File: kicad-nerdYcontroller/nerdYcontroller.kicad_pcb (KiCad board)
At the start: 4 copper layers, 69.8 x 35.2 mm, 124 parts, among them J201 S2B-PH-SM4-TB, J301 Conn_02x03_Odd_Even, J302 Conn_02x03_Odd_Even, J303 ZX-HY2.0-4PLT, J304 HLE-115-02-F-DV, P201 USB_C_Plug_USB2.0, Q301 DDTC113ZCA, U101 RP2040, U102 W25Q128JVS, U201 AMS1117-3.3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

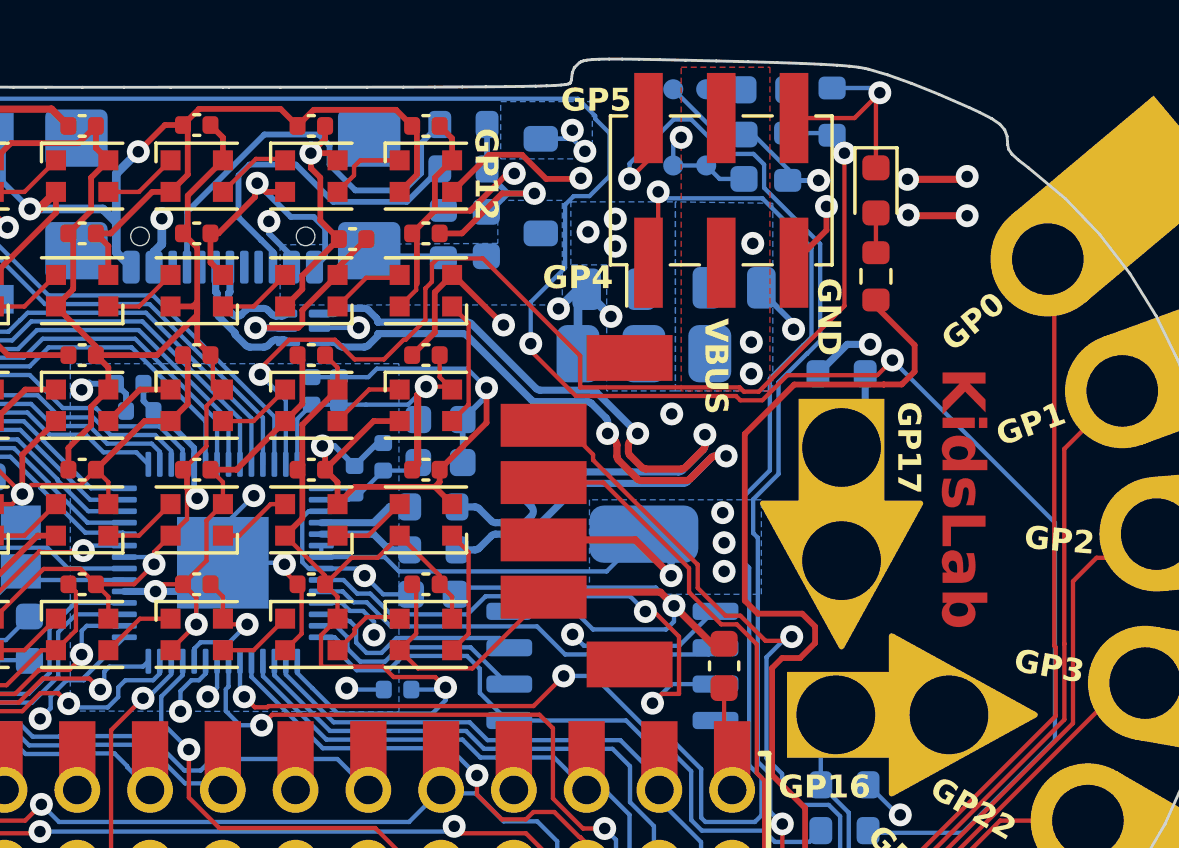
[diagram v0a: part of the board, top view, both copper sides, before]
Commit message: fixing missing usb-c 2-way connectivity
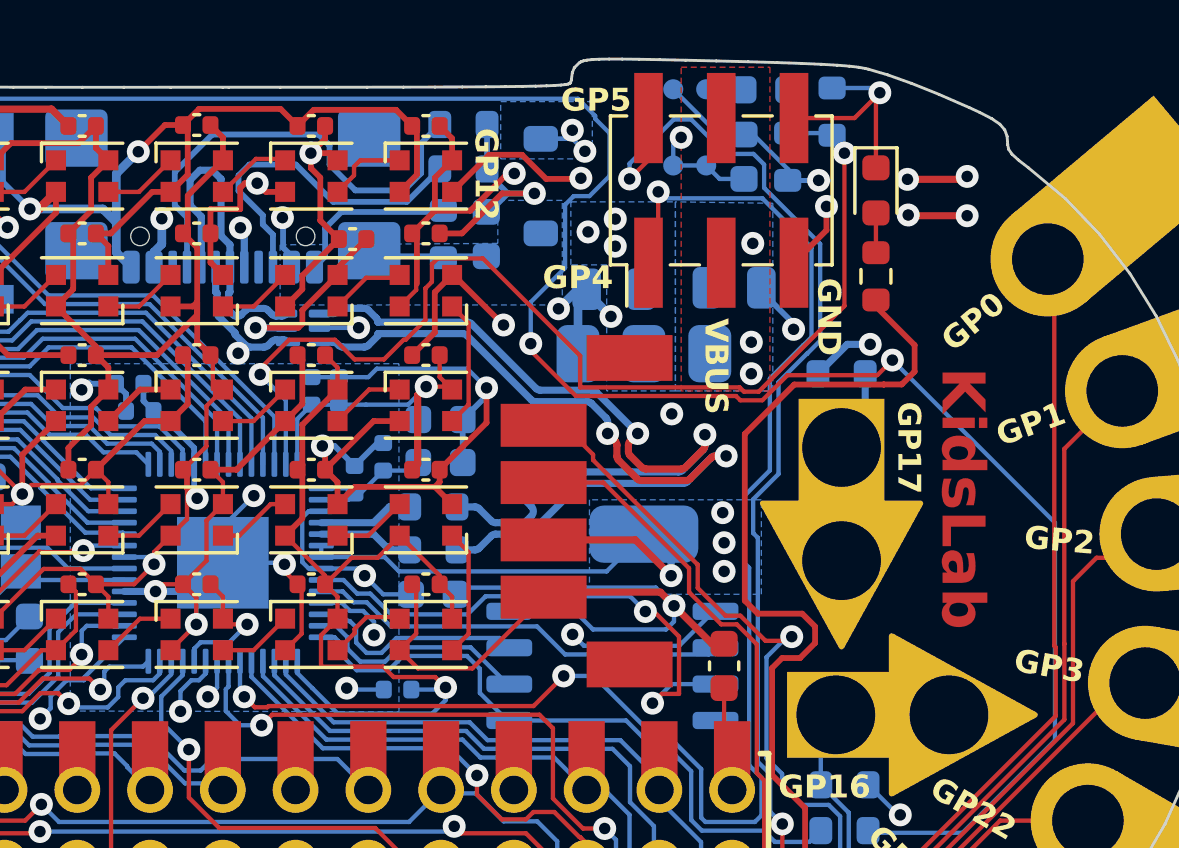
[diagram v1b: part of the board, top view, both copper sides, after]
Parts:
- removed REF**: OSHW-Logo_5.7x6mm_SilkScreen, Symbol:OSHW-Logo_5.7x6mm_SilkScreen
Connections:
- P201 pad B6: (no net) -> /power-and-usb/USBC-D+
- P201 pad B7: (no net) -> /power-and-usb/USBC-D-
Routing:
- net /power-and-usb/USBC-D+: track 4.76 -> 12.9 mm, vias 0 -> 2
- net /power-and-usb/USBC-D-: track 3.82 -> 11.6 mm
- net GND: track 308.4 -> 310.4 mm
- net Net-(P201-CC): track 14.6 -> 16.1 mm
- net /power-and-usb/usb_vcc: track 14.6 -> 15.7 mm
